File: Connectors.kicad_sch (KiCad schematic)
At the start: 4 parts, among them J4 Conn_02x03_Odd_Even

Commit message: Symbol to footprint associations are completed.
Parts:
- J1, J2: value ~ -> Conn_01x04_Male; footprint (none) -> Connector_PinHeader_2.54mm:PinHeader_1x04_P2.54mm_Vertical
- J3: value ~ -> Conn_01x09_Male; footprint (none) -> Connector_PinHeader_2.54mm:PinHeader_1x09_P2.54mm_Vertical
- J4: footprint (none) -> Connector_PinHeader_2.54mm:PinHeader_2x03_P2.54mm_Vertical
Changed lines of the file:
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@@
 			)
 		)
-		(property "Value" "~"
+		(property "Value" "Conn_01x04_Male"
 			(at 97.4745 60.96 0)
 			(effects
@@
 					(size 1.27 1.27)
 				)
-			)
-		)
-		(property "Footprint" ""
+				(hide yes)
+			)
+		)
+		(property "Footprint" "Connector_PinHeader_2.54mm:PinHeader_1x04_P2.54mm_Vertical"
 			(at 97.79 59.69 0)
 			(effects
@@
 			)
 		)
-		(property "Value" "~"
+		(property "Value" "Conn_01x04_Male"
 			(at 122.8745 59.69 0)
 			(effects
@@
 					(size 1.27 1.27)
 				)
-			)
-		)
-		(property "Footprint" ""
+				(hide yes)
+			)
+		)
+		(property "Footprint" "Connector_PinHeader_2.54mm:PinHeader_1x04_P2.54mm_Vertical"
 			(at 123.19 58.42 0)
 			(effects
@@
 			)
 		)
-		(property "Value" "~"
+		(property "Value" "Conn_01x09_Male"
 			(at 97.4317 78.74 0)
 			(effects
@@
 					(size 1.27 1.27)
 				)
-			)
-		)
-		(property "Footprint" ""
+				(hide yes)
+			)
+		)
+		(property "Footprint" "Connector_PinHeader_2.54mm:PinHeader_1x09_P2.54mm_Vertical"
 			(at 97.79 77.47 0)
 			(effects
@@
 			)
 		)
-		(property "Footprint" ""
+		(property "Footprint" "Connector_PinHeader_2.54mm:PinHeader_2x03_P2.54mm_Vertical"
 			(at 120.65 86.36 0)
 			(effects

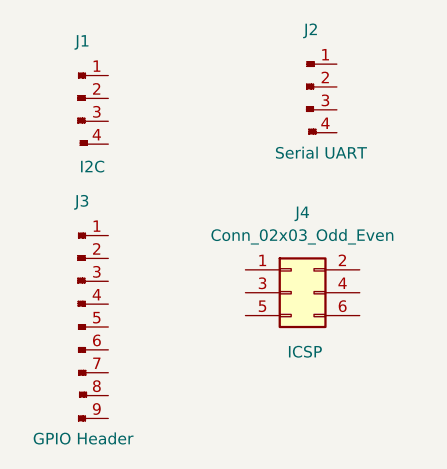
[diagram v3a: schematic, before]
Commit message: Second sheets connections are done.
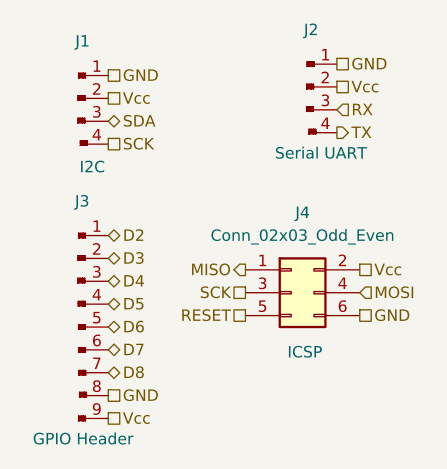
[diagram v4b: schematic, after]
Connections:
- net GND: now reaches J1.1
- net GND: now also J2.1, J3.8, J4.6 (Pin_6)
- net Vcc: now reaches J1.2
- net Vcc: now also J2.2, J3.9, J4.2 (Pin_2)
- net SDA: now reaches J1.3
- net SCK: now reaches J1.4
- net SCK: now also J4.3 (Pin_3)
- net RX: now reaches J2.3
- net TX: now reaches J2.4
- net D2: now reaches J3.1
- net D3: now reaches J3.2
- net D4: now reaches J3.3
- net D5: now reaches J3.4
- net D6: now reaches J3.5
- net D7: now reaches J3.6
- net D8: now reaches J3.7
- net MISO: now reaches J4.1 (Pin_1)
- net MOSI: now reaches J4.4 (Pin_4)
- net RESET: now reaches J4.5 (Pin_5)

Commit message: Fixed two defects in the schematic.
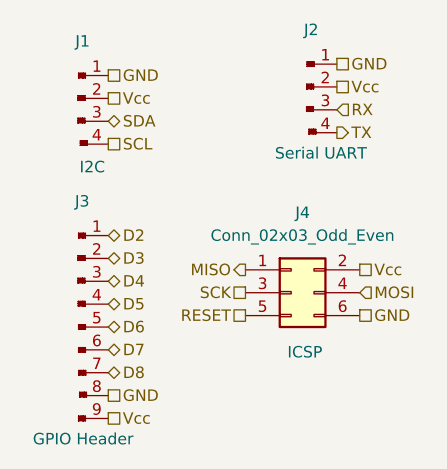
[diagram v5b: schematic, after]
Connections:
- net SCK: no longer J1.4
- new net SCL: J1.4
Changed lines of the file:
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@@
 		)
 	)
-	(hierarchical_label "SCK"
+	(hierarchical_label "SCL"
 		(shape passive)
 		(at 100.33 69.85 0)
